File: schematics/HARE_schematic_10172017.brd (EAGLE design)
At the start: 105.1 x 80 mm, 86 parts, among them IC1 NE5532N, IC2 NE5532N, IC3 FT232RL, IC4 NE5532N, IC5 7805DT, J2 STEREOSW, J3 STEREOSW, Q1 16 MHz, SW1 3PDTBLUE, SW2 Reset Button, U1 ATMEGA328P-PU, X2 USB-B-H

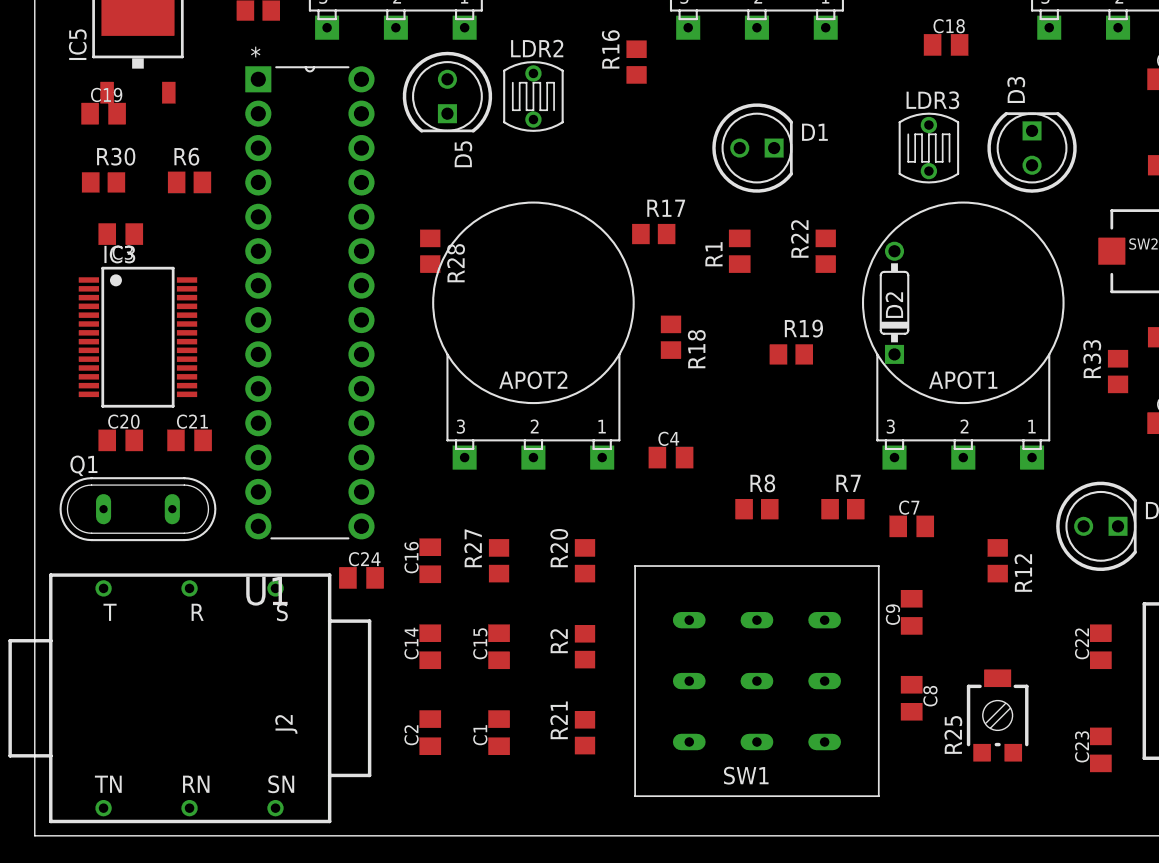
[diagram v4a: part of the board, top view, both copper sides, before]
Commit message: Added DAC_OUT node to schematic
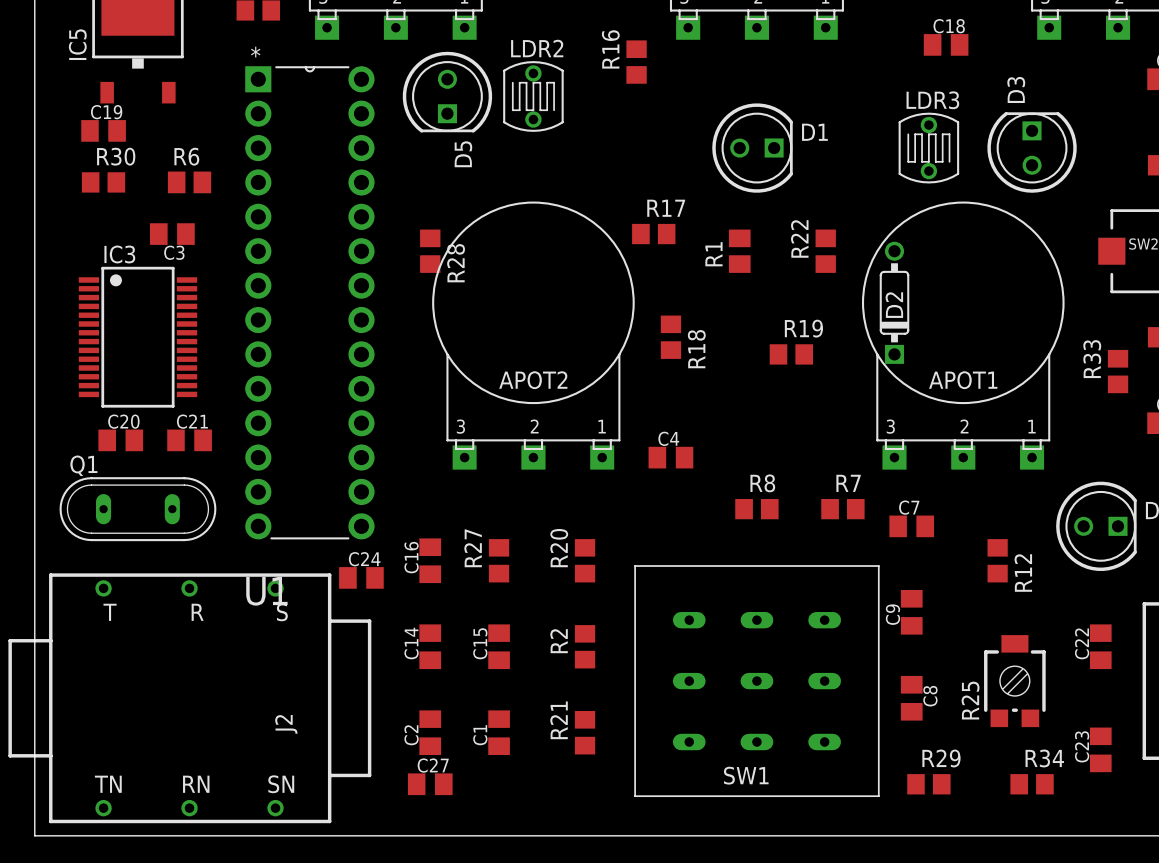
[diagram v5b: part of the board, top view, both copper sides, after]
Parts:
- added C27: 4.7nF, resistor:C0805K
- added R29: 1MEG, resistor:R0805
- added R34: 3.9k, resistor:R0805
- moved C3 3.81 mm to (10.2, 44.5)
- moved R25 2.84 mm to (72.4, 11.4)
- moved C19 1.27 mm to (5.08, 52.1)
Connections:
- removed net N$35: C14.2
- removed net N$39: C17.2
- new net N$50: R29.2, U1.16
- new net N$55: R34.2, U1.15
- net DAC_OUT: now also C27.2, R29.1, R34.1
- net GND: now also C27.1
- net VCA_IN: now also C14.2
- net VCA_OUT: now also C17.2
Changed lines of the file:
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@@
 <element name="R5" library="rcl" package="M0805" value="10k" x="102.87" y="48.26" rot="R90"/>
 <element name="R6" library="rcl" package="M0805" value="10k" x="11.43" y="48.26"/>
-<element name="C3" library="resistor" package="C0805K" value="10uF" x="6.35" y="44.45" rot="R180"/>
+<element name="C3" library="resistor" package="C0805K" value="10uF" x="10.16" y="44.45" rot="R180"/>
 <element name="R7" library="resistor" package="R0805" value="1k" x="59.69" y="24.13"/>
 <element name="R8" library="resistor" package="R0805" value="1k" x="53.34" y="24.13"/>
@@
 <element name="D4" library="gm-diodes" package="LED5MM" value="LED5MM" x="78.74" y="22.86"/>
 <element name="D5" library="gm-diodes" package="LED5MM" value="LED5MM" x="30.48" y="54.61" rot="R270"/>
-<element name="R25" library="resistor" package="RTRIM3314G" value="10k" x="71.12" y="8.89"/>
+<element name="R25" library="resistor" package="RTRIM3314G" value="10k" x="72.39" y="11.43"/>
 <element name="IC5" library="gm-regulators" package="TO252" value="7805DT" x="7.62" y="59.69"/>
-<element name="C19" library="resistor" package="C0805K" value="10uF" x="5.08" y="53.34"/>
+<element name="C19" library="resistor" package="C0805K" value="10uF" x="5.08" y="52.07"/>
 <element name="Q1" library="special" package="QS" value="16 MHz" x="7.62" y="24.13"/>
 <element name="J2" library="gm-jacks" package="NMJ6HCD2" value="STEREOSW" x="11.43" y="10.16"/>
@@
 <element name="SW2" library="adafruit" package="PUSHBUTTON_SMD_SJ" value="Reset Button" x="82.55" y="43.18"/>
 <element name="R33" library="resistor" package="R0805" value="10k" x="80.01" y="34.29" rot="R90"/>
+<element name="R29" library="resistor" package="R0805" value="1MEG" x="66.04" y="3.81"/>
+<element name="R34" library="resistor" package="R0805" value="3.9k" x="73.66" y="3.81"/>
+<element name="C27" library="resistor" package="C0805K" value="4.7nF" x="29.21" y="3.81"/>
 </elements>
 <signals>
@@
 <contactref element="C26" pad="1"/>
 <contactref element="SW2" pad="P$1"/>
+<contactref element="C27" pad="1"/>
 <wire x1="97.79" y1="64.77" x2="97.79" y2="70.66" width="0" layer="19" extent="1-1"/>
 <wire x1="85.09" y1="59.69" x2="97.79" y2="64.77" width="0" layer="19" extent="1-1"/>
@@
 <wire x1="66.04" y1="52.5018" x2="73.66" y2="52.07" width="0" layer="19" extent="1-1"/>
 <wire x1="58.42" y1="59.69" x2="66.04" y2="52.5018" width="0" layer="19" extent="1-1"/>
-<wire x1="97.79" y1="49.53" x2="97.79" y2="64.77" width="0" layer="19" extent="1-1"/>
-<wire x1="97.79" y1="34.29" x2="97.79" y2="49.53" width="0" layer="19" extent="1-1"/>
+<wire x1="49.8" y1="69.85" x2="58.42" y2="59.69" width="0" layer="19" extent="1-1"/>
+<wire x1="85.55" y1="43.18" x2="73.66" y2="52.07" width="0" layer="19" extent="1-1"/>
+<wire x1="97.79" y1="49.53" x2="85.55" y2="43.18" width="0" layer="19" extent="1-1"/>
+<wire x1="97.79" y1="34.29" x2="85.55" y2="43.18" width="0" layer="19" extent="1-1"/>
 <wire x1="95.25" y1="19.545" x2="97.79" y2="34.29" width="0" layer="19" extent="1-1"/>
 <wire x1="88.9" y1="19.545" x2="95.25" y2="19.545" width="0" layer="19" extent="1-1"/>
@@
 <wire x1="7.62" y1="62.19" x2="15.51" y2="64.77" width="0" layer="19" extent="1-1"/>
 <wire x1="7.64" y1="71.12" x2="7.62" y2="62.19" width="0" layer="19" extent="1-1"/>
-<wire x1="4.08" y1="53.34" x2="7.62" y2="62.19" width="0" layer="19" extent="1-1"/>
-<wire x1="7.35" y1="44.45" x2="4.08" y2="53.34" width="0" layer="19" extent="1-1"/>
-<wire x1="11.245" y1="39.755" x2="7.35" y2="44.45" width="0" layer="19" extent="1-1"/>
+<wire x1="4.08" y1="52.07" x2="7.62" y2="62.19" width="0" layer="19" extent="1-1"/>
+<wire x1="12.38" y1="48.26" x2="4.08" y2="52.07" width="0" layer="19" extent="1-1"/>
+<wire x1="11.16" y1="44.45" x2="12.38" y2="48.26" width="0" layer="19" extent="1-1"/>
+<wire x1="11.245" y1="39.755" x2="11.16" y2="44.45" width="0" layer="19" extent="1-1"/>
 <wire x1="11.245" y1="39.105" x2="11.245" y2="39.755" width="0" layer="19" extent="1-1"/>
 <wire x1="11.245" y1="36.505" x2="11.245" y2="39.105" width="0" layer="19" extent="1-1"/>
@@
 <wire x1="10.43" y1="29.21" x2="11.245" y2="34.555" width="0" layer="19" extent="1-1"/>
 <wire x1="5.35" y1="29.21" x2="10.43" y2="29.21" width="0" layer="19" extent="1-1"/>
-<wire x1="12.38" y1="48.26" x2="7.35" y2="44.45" width="0" layer="19" extent="1-1"/>
 <wire x1="3.995" y1="37.155" x2="11.245" y2="36.505" width="0" layer="19" extent="1-1"/>
 <wire x1="11.43" y1="18.275" x2="10.43" y2="29.21" width="0" layer="19" extent="1-1"/>
@@
 <wire x1="17.78" y1="2.045" x2="17.78" y2="18.275" width="0" layer="19" extent="1-1"/>
 <wire x1="11.43" y1="2.045" x2="17.78" y2="2.045" width="0" layer="19" extent="1-1"/>
-<wire x1="49.8" y1="69.85" x2="11.43" y2="2.045" width="0" layer="19" extent="1-1"/>
-<wire x1="85.55" y1="43.18" x2="49.8" y2="69.85" width="0" layer="19" extent="1-1"/>
+<wire x1="28.21" y1="3.81" x2="11.43" y2="2.045" width="0" layer="19" extent="1-1"/>
 </signal>
 <signal name="INPUT">
@@
 <wire x1="102.87" y1="49.21" x2="90.17" y2="34.29" width="0" layer="19" extent="1-1"/>
 <wire x1="10.48" y1="48.26" x2="102.87" y2="49.21" width="0" layer="19" extent="1-1"/>
-<wire x1="5.35" y1="44.45" x2="10.48" y2="48.26" width="0" layer="19" extent="1-1"/>
+<wire x1="9.16" y1="44.45" x2="10.48" y2="48.26" width="0" layer="19" extent="1-1"/>
 </signal>
 <signal name="N$12">
@@
 <signal name="DAC_OUT">
 <contactref element="C8" pad="2"/>
+<contactref element="R34" pad="1"/>
+<contactref element="R29" pad="1"/>
+<contactref element="C27" pad="2"/>
+<wire x1="65.09" y1="3.81" x2="64.77" y2="9.16" width="0" layer="19" extent="1-1"/>
+<wire x1="72.71" y1="3.81" x2="65.09" y2="3.81" width="0" layer="19" extent="1-1"/>
+<wire x1="30.21" y1="3.81" x2="72.71" y2="3.81" width="0" layer="19" extent="1-1"/>
 </signal>
 <signal name="VCF_IN">
@@
 <wire x1="21.59" y1="59.69" x2="35.1282" y2="64.77" width="0" layer="19" extent="1-1"/>
 <wire x1="9.9" y1="54.89" x2="21.59" y2="59.69" width="0" layer="19" extent="1-1"/>
-<wire x1="6.08" y1="53.34" x2="9.9" y2="54.89" width="0" layer="19" extent="1-1"/>
+<wire x1="6.08" y1="52.07" x2="9.9" y2="54.89" width="0" layer="19" extent="1-1"/>
 <wire x1="7.64" y1="69.1388" x2="9.9" y2="54.89" width="0" layer="19" extent="1-1"/>
 <wire x1="16.51" y1="40.64" x2="9.9" y2="54.89" width="0" layer="19" extent="1-1"/>
@@
 <signal name="VCA_IN">
 <contactref element="C13" pad="1"/>
+<contactref element="C14" pad="2"/>
+<wire x1="29.21" y1="14.97" x2="41.91" y2="70.85" width="0" layer="19" extent="1-1"/>
 </signal>
 <signal name="N$28">
@@
 <wire x1="29.21" y1="21.32" x2="40.64" y2="21.27" width="0" layer="19" extent="1-1"/>
 </signal>
-<signal name="N$35">
-<contactref element="C14" pad="2"/>
-</signal>
 <signal name="VCA_OUT">
 <contactref element="C16" pad="1"/>
+<contactref element="C17" pad="2"/>
+<wire x1="29.21" y1="19.32" x2="88.63" y2="67.31" width="0" layer="19" extent="1-1"/>
 </signal>
 <signal name="ADC_IN">
@@
 <contactref element="C2" pad="1"/>
 <contactref element="R25" pad="1"/>
-<wire x1="97.79" y1="57.15" x2="72.27" y2="6.14" width="0" layer="19" extent="1-1"/>
+<wire x1="97.79" y1="57.15" x2="73.54" y2="8.68" width="0" layer="19" extent="1-1"/>
 <wire x1="29.21" y1="6.62" x2="97.79" y2="57.15" width="0" layer="19" extent="1-1"/>
 </signal>
 <signal name="N$38">
 <contactref element="IC4" pad="3"/>
-</signal>
-<signal name="N$39">
-<contactref element="C17" pad="2"/>
 </signal>
 <signal name="N$40">
@@
 <contactref element="R25" pad="3"/>
 <contactref element="R25" pad="2"/>
-<wire x1="71.12" y1="11.64" x2="69.97" y2="6.14" width="0" layer="19" extent="1-1"/>
-<wire x1="102.87" y1="54.93" x2="71.12" y2="11.64" width="0" layer="19" extent="1-1"/>
+<wire x1="72.39" y1="14.18" x2="71.24" y2="8.68" width="0" layer="19" extent="1-1"/>
+<wire x1="102.87" y1="54.93" x2="72.39" y2="14.18" width="0" layer="19" extent="1-1"/>
 </signal>
 <signal name="OSC">
@@
 <wire x1="3.995" y1="34.555" x2="16.51" y2="48.26" width="0" layer="19" extent="1-1"/>
 </signal>
+<signal name="N$55">
+<contactref element="R34" pad="2"/>
+<contactref element="U1" pad="15"/>
+<wire x1="74.61" y1="3.81" x2="24.13" y2="22.86" width="0" layer="19" extent="1-1"/>
+</signal>
+<signal name="N$50">
+<contactref element="U1" pad="16"/>
+<contactref element="R29" pad="2"/>
+<wire x1="66.99" y1="3.81" x2="24.13" y2="25.4" width="0" layer="19" extent="1-1"/>
+</signal>
 </signals>

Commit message: Fixed ERC errors
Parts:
- added R35, R36: 1k, resistor:R0805
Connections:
- removed net N$24: IC2.3
- removed net N$28: IC2.5
- removed net N$38: IC4.3
- removed net N$44: IC4.5
- removed net N$62: IC3.19
- net ADC_IN: now also R35.1, R36.2
- net GND: now also R36.1
- net RESET#: now also IC3.19
- net VCC: now also R35.2
- net V_BIAS: now also IC2.3, IC2.5, IC4.3, IC4.5
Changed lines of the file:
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@@
 <element name="R34" library="resistor" package="R0805" value="3.9k" x="73.66" y="3.81"/>
 <element name="C27" library="resistor" package="C0805K" value="4.7nF" x="29.21" y="3.81"/>
+<element name="R35" library="resistor" package="R0805" value="1k" x="-11.43" y="-7.62"/>
+<element name="R36" library="resistor" package="R0805" value="1k" x="-11.43" y="-13.97"/>
 </elements>
 <signals>
@@
 <contactref element="IC5" pad="1"/>
 <contactref element="C25" pad="2"/>
+<contactref element="R35" pad="2"/>
 <wire x1="92.99" y1="73.66" x2="97.79" y2="76.66" width="0" layer="19" extent="1-1"/>
 <wire x1="90.17" y1="57.15" x2="92.99" y2="73.66" width="0" layer="19" extent="1-1"/>
@@
 <wire x1="90.17" y1="26.67" x2="90.17" y2="41.91" width="0" layer="19" extent="1-1"/>
 <wire x1="52.07" y1="42.23" x2="90.17" y2="41.91" width="0" layer="19" extent="1-1"/>
-<wire x1="5.34" y1="54.89" x2="52.07" y2="42.23" width="0" layer="19" extent="1-1"/>
-<wire x1="17.51" y1="64.77" x2="5.34" y2="54.89" width="0" layer="19" extent="1-1"/>
+<wire x1="17.51" y1="64.77" x2="52.07" y2="42.23" width="0" layer="19" extent="1-1"/>
+<wire x1="5.34" y1="54.89" x2="17.51" y2="64.77" width="0" layer="19" extent="1-1"/>
+<wire x1="-10.48" y1="-7.62" x2="5.34" y2="54.89" width="0" layer="19" extent="1-1"/>
 </signal>
 <signal name="GND">
@@
 <contactref element="SW2" pad="P$1"/>
 <contactref element="C27" pad="1"/>
+<contactref element="R36" pad="1"/>
 <wire x1="97.79" y1="64.77" x2="97.79" y2="70.66" width="0" layer="19" extent="1-1"/>
 <wire x1="85.09" y1="59.69" x2="97.79" y2="64.77" width="0" layer="19" extent="1-1"/>
@@
 <wire x1="17.78" y1="18.275" x2="11.43" y2="18.275" width="0" layer="19" extent="1-1"/>
 <wire x1="23.13" y1="19.05" x2="17.78" y2="18.275" width="0" layer="19" extent="1-1"/>
-<wire x1="17.78" y1="2.045" x2="17.78" y2="18.275" width="0" layer="19" extent="1-1"/>
+<wire x1="28.21" y1="3.81" x2="23.13" y2="19.05" width="0" layer="19" extent="1-1"/>
+<wire x1="17.78" y1="2.045" x2="28.21" y2="3.81" width="0" layer="19" extent="1-1"/>
 <wire x1="11.43" y1="2.045" x2="17.78" y2="2.045" width="0" layer="19" extent="1-1"/>
-<wire x1="28.21" y1="3.81" x2="11.43" y2="2.045" width="0" layer="19" extent="1-1"/>
+<wire x1="-12.38" y1="-13.97" x2="11.43" y2="2.045" width="0" layer="19" extent="1-1"/>
 </signal>
 <signal name="INPUT">
@@
 <contactref element="IC1" pad="3"/>
 <contactref element="IC1" pad="5"/>
-<wire x1="90.17" y1="34.29" x2="97.79" y2="31.75" width="0" layer="19" extent="1-1"/>
-<wire x1="102.87" y1="49.21" x2="90.17" y2="34.29" width="0" layer="19" extent="1-1"/>
-<wire x1="10.48" y1="48.26" x2="102.87" y2="49.21" width="0" layer="19" extent="1-1"/>
+<contactref element="IC2" pad="3"/>
+<contactref element="IC2" pad="5"/>
+<contactref element="IC4" pad="5"/>
+<contactref element="IC4" pad="3"/>
+<wire x1="90.17" y1="64.77" x2="97.79" y2="62.23" width="0" layer="19" extent="1-1"/>
+<wire x1="102.87" y1="49.21" x2="97.79" y2="62.23" width="0" layer="19" extent="1-1"/>
+<wire x1="97.79" y1="46.99" x2="102.87" y2="49.21" width="0" layer="19" extent="1-1"/>
+<wire x1="90.17" y1="49.53" x2="97.79" y2="46.99" width="0" layer="19" extent="1-1"/>
+<wire x1="90.17" y1="34.29" x2="97.79" y2="46.99" width="0" layer="19" extent="1-1"/>
+<wire x1="97.79" y1="31.75" x2="90.17" y2="34.29" width="0" layer="19" extent="1-1"/>
+<wire x1="10.48" y1="48.26" x2="90.17" y2="49.53" width="0" layer="19" extent="1-1"/>
 <wire x1="9.16" y1="44.45" x2="10.48" y2="48.26" width="0" layer="19" extent="1-1"/>
 </signal>
@@
 <wire x1="36.83" y1="75.2" x2="63.5" y2="43.18" width="0" layer="19" extent="1-1"/>
 <wire x1="48.26" y1="75.93" x2="36.83" y2="75.2" width="0" layer="19" extent="1-1"/>
-</signal>
-<signal name="N$24">
-<contactref element="IC2" pad="3"/>
 </signal>
 <signal name="N$26">
@@
 <wire x1="29.21" y1="14.97" x2="41.91" y2="70.85" width="0" layer="19" extent="1-1"/>
 </signal>
-<signal name="N$28">
-<contactref element="IC2" pad="5"/>
-</signal>
 <signal name="N$30">
 <contactref element="C14" pad="1"/>
@@
 <contactref element="R21" pad="2"/>
 <contactref element="U1" pad="23"/>
+<contactref element="R36" pad="2"/>
+<contactref element="R35" pad="1"/>
 <wire x1="40.64" y1="8.57" x2="24.13" y2="43.18" width="0" layer="19" extent="1-1"/>
+<wire x1="-12.38" y1="-7.62" x2="40.64" y2="8.57" width="0" layer="19" extent="1-1"/>
+<wire x1="-10.48" y1="-13.97" x2="-12.38" y2="-7.62" width="0" layer="19" extent="1-1"/>
 </signal>
 <signal name="DRY">
@@
 <wire x1="29.21" y1="6.62" x2="97.79" y2="57.15" width="0" layer="19" extent="1-1"/>
 </signal>
-<signal name="N$38">
-<contactref element="IC4" pad="3"/>
-</signal>
 <signal name="N$40">
 <contactref element="C17" pad="1"/>
@@
 <wire x1="90.17" y1="59.69" x2="68.46" y2="63.29" width="0" layer="19" extent="1-1"/>
 </signal>
-<signal name="N$44">
-<contactref element="IC4" pad="5"/>
-</signal>
 <signal name="N$45">
 <contactref element="C18" pad="1"/>
@@
 <wire x1="75.25" y1="71.12" x2="73.66" y2="49.53" width="0" layer="19" extent="1-1"/>
 </signal>
-<signal name="N$62">
-<contactref element="IC3" pad="19"/>
-</signal>
 <signal name="N$63">
 <contactref element="D6" pad="A"/>
@@
 <contactref element="SW2" pad="P$2"/>
 <contactref element="R33" pad="2"/>
-<wire x1="79.55" y1="43.18" x2="80.01" y2="35.24" width="0" layer="19" extent="1-1"/>
-<wire x1="15.56" y1="60.96" x2="79.55" y2="43.18" width="0" layer="19" extent="1-1"/>
-<wire x1="16.51" y1="55.88" x2="15.56" y2="60.96" width="0" layer="19" extent="1-1"/>
+<contactref element="IC3" pad="19"/>
+<wire x1="80.01" y1="35.24" x2="79.55" y2="43.18" width="0" layer="19" extent="1-1"/>
+<wire x1="16.51" y1="55.88" x2="79.55" y2="43.18" width="0" layer="19" extent="1-1"/>
+<wire x1="15.56" y1="60.96" x2="16.51" y2="55.88" width="0" layer="19" extent="1-1"/>
+<wire x1="11.245" y1="35.205" x2="16.51" y2="55.88" width="0" layer="19" extent="1-1"/>
 </signal>
 <signal name="RTS#">
